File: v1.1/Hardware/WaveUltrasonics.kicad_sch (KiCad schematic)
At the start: 0 parts

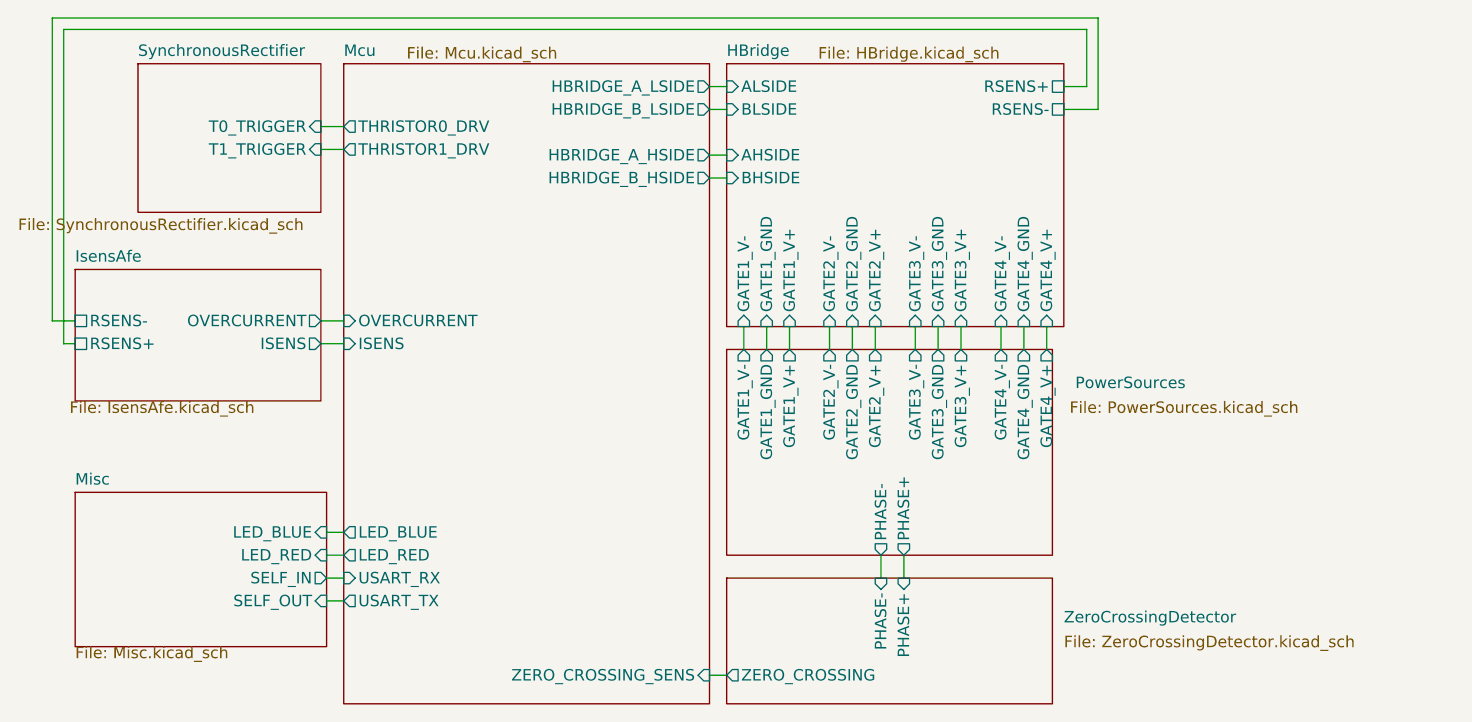
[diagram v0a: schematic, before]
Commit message: v1.1&v1.2 PCB addition.
#####v1.1#####
+Change of MCU; STM32F334C8T6 instead of STM32F103C8T6.
+Filtering 3rd order components of the square wave.
+Use  4 capacitors.
+Adapted to generic transformer(primary 6.4mH, secondary 14.4mH)
+Faster IGBT.

########v1.2#######
+Measures only PZT current and voltage.
+Differential inputs.
+Analog circuitry is capable of measuring four quadrant voltage, current and complex impedance.
+Half bridge configuration.
+Gate resistance of the IGBT's lowered.
+Only USART based touch panel can be connected; not conventional LCD.
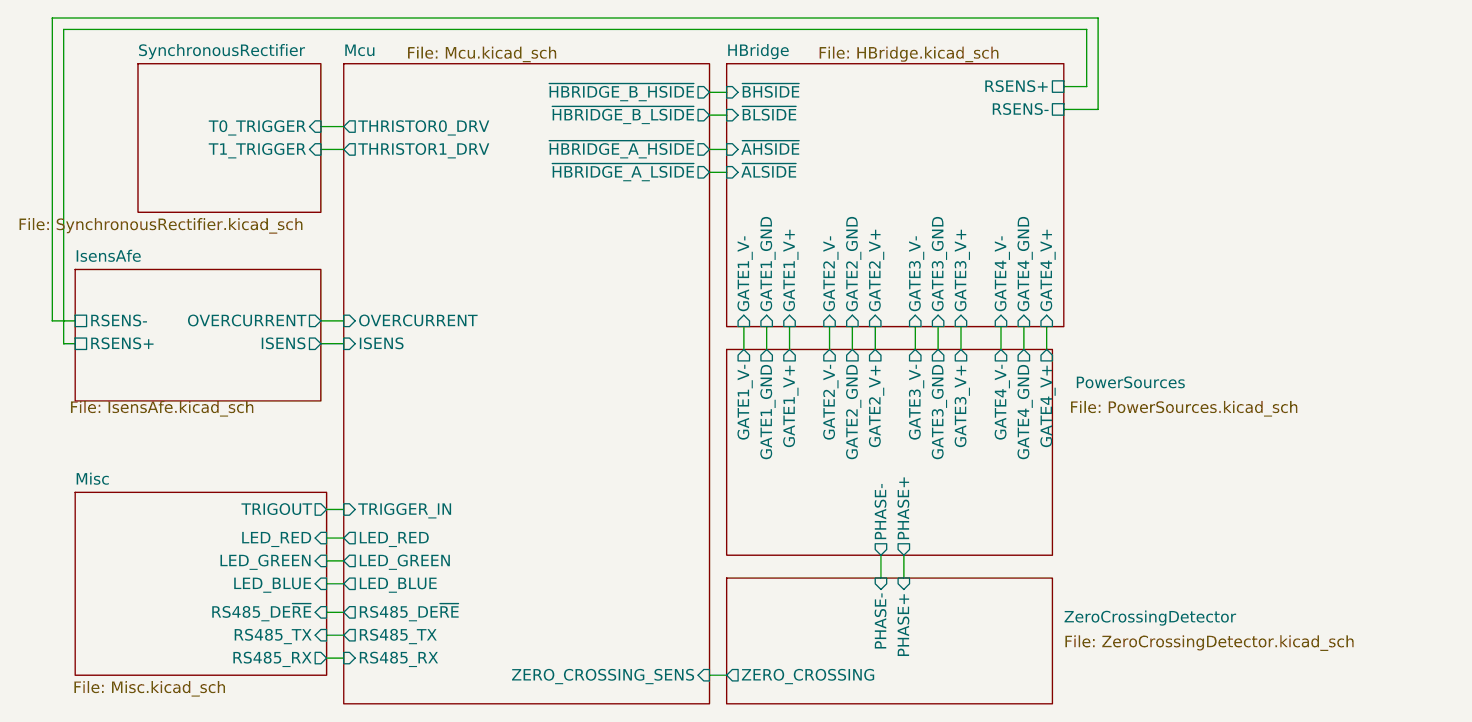
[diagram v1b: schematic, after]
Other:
- sheet HBridge ports: added ~AHSIDE, ~ALSIDE, ~BHSIDE, ~BLSIDE; removed AHSIDE, ALSIDE, BHSIDE, BLSIDE
- sheet Mcu ports: added LED_GREEN, RS485_DE~RE, RS485_RX, RS485_TX, TRIGGER_IN, ~HBRIDGE_A_HSIDE, ~HBRIDGE_A_LSIDE, ~HBRIDGE_B_HSIDE, ~HBRIDGE_B_LSIDE; removed HBRIDGE_A_HSIDE, HBRIDGE_A_LSIDE, HBRIDGE_B_HSIDE, HBRIDGE_B_LSIDE, USART_RX, USART_TX
- sheet Misc ports: added LED_GREEN, RS485_DE~RE, RS485_RX, RS485_TX, TRIGOUT; removed SELF_IN, SELF_OUT
